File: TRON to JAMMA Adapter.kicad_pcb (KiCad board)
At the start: 2 copper layers, 111 x 98.7 mm, 58 parts, among them P1 1K, P2 10K, P3 1K, U1 74LS86, U2A 74LS191, U2B 74LS191, U3 NE555, U4 LM386, U5 NE555

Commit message: move connectors up, rework vias a bit, update text
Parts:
- moved MCRJ2 3.80 mm to (153.8, 66.6)
- moved MCRJ3 3.80 mm to (168.8, 66.6)
- moved MCRJ4A 3.80 mm to (98.0, 66.6)
- moved MCRJ4B 3.80 mm to (118.2, 66.6)
- moved MCRJ5 3.80 mm to (138.6, 66.6)
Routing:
- net 1P_U: track 30.5 -> 24.9 mm
- net VOL_GND: track 33.0 -> 38.3 mm
- net 1P_B1: track 30.2 -> 25.4 mm
- net 2P_START: track 49.6 -> 45.4 mm
- net 1P_D: track 32.0 -> 28.1 mm
- net E3: track 32.3 -> 36.1 mm
- net VOL_IN: track 30.6 -> 34.4 mm
- net VIDEO_RED: track 19.9 -> 16.1 mm
- net VOL_OUT: track 27.6 -> 31.4 mm
- net VIDEO_VSYNC: track 76.5 -> 80.3 mm
- net VIDEO_G: track 20.0 -> 16.2 mm
- net E4: track 32.7 -> 36.5 mm
- net E2: track 31.3 -> 35.1 mm
- net AUDIO_R: track 41.6 -> 45.4 mm
- net E1: track 30.7 -> 34.5 mm
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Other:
- board text added: "Bally/Midway MCR II JAMMA Interface for TRON^{TM}, Discs of TRON^{TM}, Rev. 1"
- board text added: "COIN 1"
- board text added: "COIN 2"
- board text removed: "Bally/Midway MCR JAMMA Interface, Rev. 1 for TRON^{TM}, Discs of TRON^{TM}"
- board text removed: "C1"
- board text removed: "C2"

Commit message: slightly widen
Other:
- board size 111 x 98.7 mm -> 111.6 x 98.7 mm
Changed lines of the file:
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@@
 	(gr_poly
 		(pts
-			(xy 173.5 56.550005) (xy 176 56.550005) (xy 176 45.05) (xy 200.500004 45.05) (xy 200.500004 68.050005)
-			(xy 200.5 68.050005) (xy 200.5 109.050005) (xy 200.5 143.75) (xy 89.5 143.75) (xy 89.5 109.050005)
-			(xy 89.499997 109.050005) (xy 89.499997 68.050005) (xy 89.499997 45.05) (xy 173.5 45.05)
+			(xy 173.5 56.550005) (xy 176 56.550005) (xy 176 45.05) (xy 200.700004 45.05) (xy 200.7 143.75) (xy 89.1 143.75)
+			(xy 89.099997 45.05) (xy 173.5 45.05)
 		)
 		(stroke

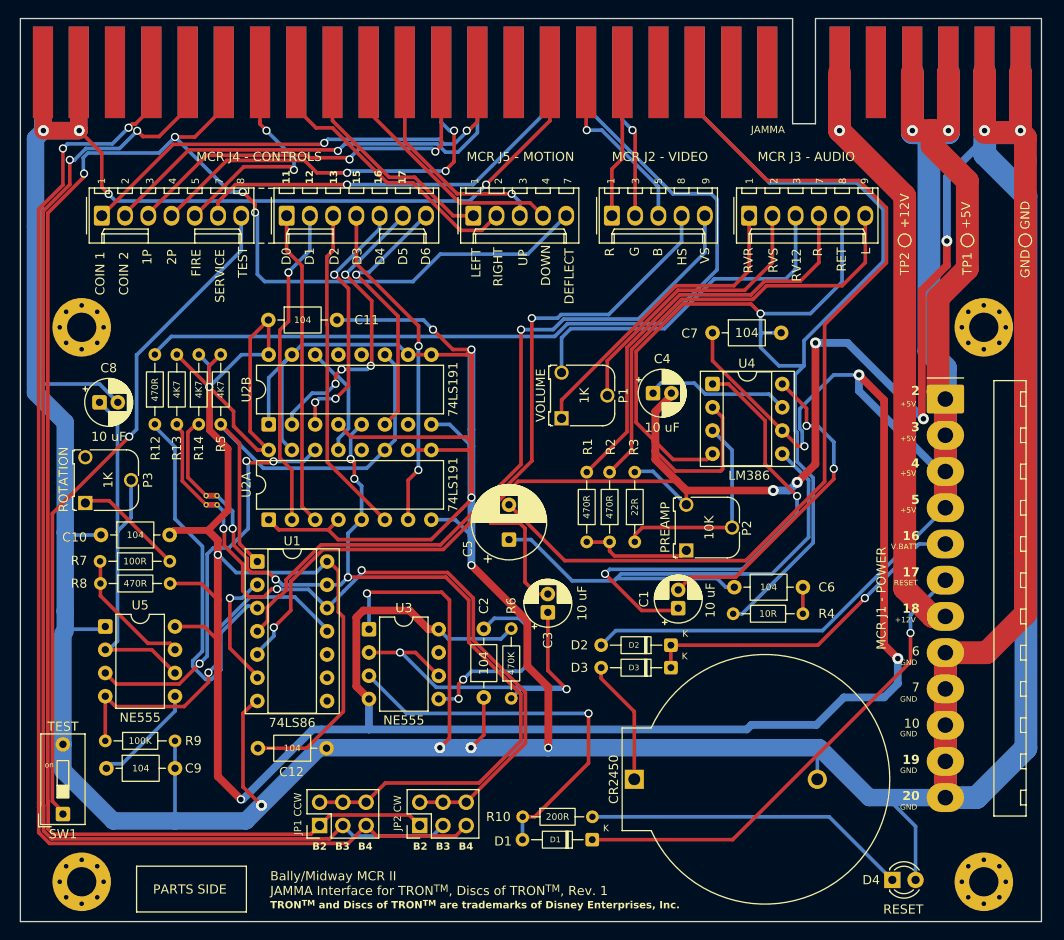
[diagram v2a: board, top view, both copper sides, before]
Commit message: slightly widen boards
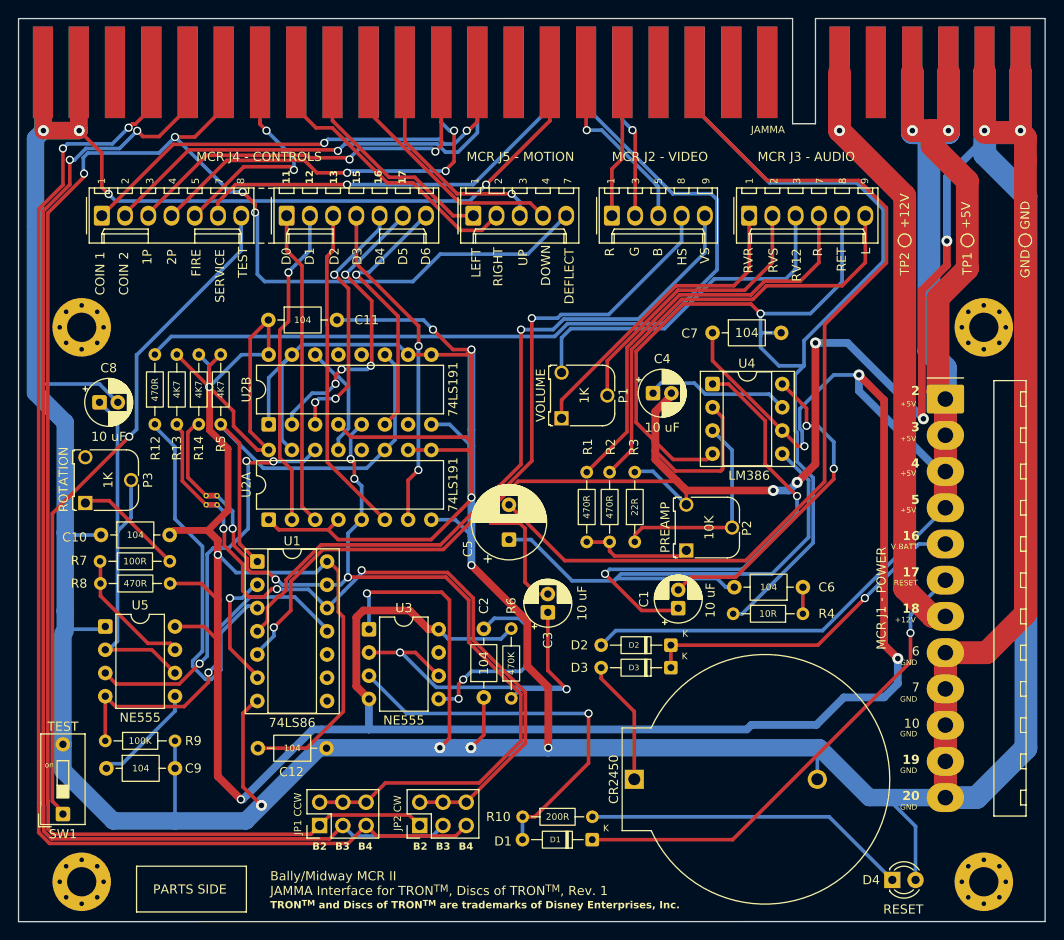
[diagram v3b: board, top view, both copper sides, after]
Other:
- board size 111.6 x 98.7 mm -> 112.2 x 98.7 mm
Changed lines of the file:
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@@
 	(gr_poly
 		(pts
-			(xy 173.5 56.550005) (xy 176 56.550005) (xy 176 45.05) (xy 200.700004 45.05) (xy 200.7 143.75) (xy 89.1 143.75)
-			(xy 89.099997 45.05) (xy 173.5 45.05)
+			(xy 173.5 56.550005) (xy 176 56.550005) (xy 176 45.05) (xy 201.100004 45.05) (xy 201.1 143.75) (xy 88.897213 143.757185)
+			(xy 88.89721 45.057185) (xy 173.5 45.05)
 		)
 		(stroke

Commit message: chamma compat, add b5/b6 and pins for level up/dn on dot
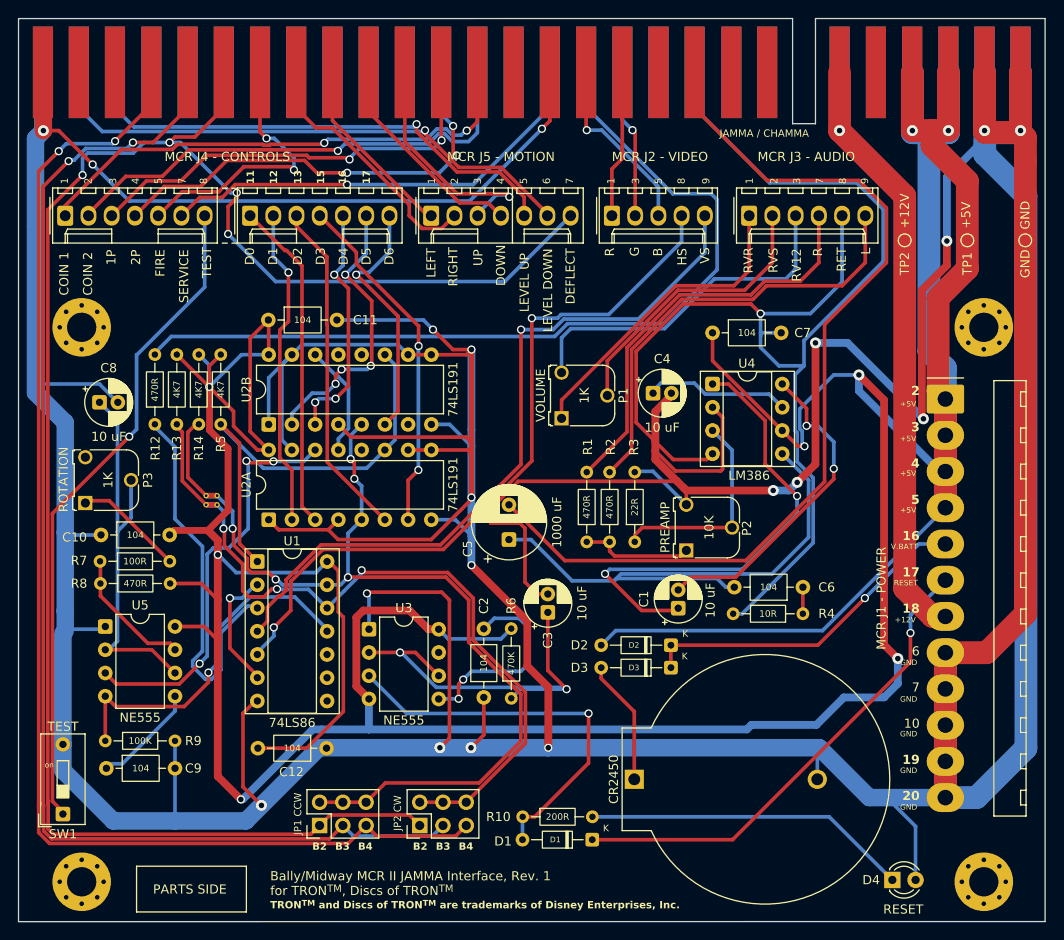
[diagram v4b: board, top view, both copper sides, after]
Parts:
- JAMMA / CHAMMA: renamed from JAMMA
- MCRJ5: value Molex_KK-254_AE-6410-05A_1x05_P2.54mm_Vertical -> Molex_KK-254_AE-6410-07A_1x07_P2.54mm_Vertical; footprint Connector_Molex:Molex_KK-254_AE-6410-05A_1x05_P2.54mm_Vertical -> Connector_Molex:Molex_KK-254_AE-6410-07A_1x07_P2.54mm_Vertical
- moved MCRJ5 4.60 mm to (134.0, 66.6)
- moved MCRJ4A 4.00 mm to (94.0, 66.6)
- moved MCRJ4B 4.00 mm to (114.2, 66.6)
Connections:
- JAMMA / CHAMMA pad 27: GND -> (no net)
- JAMMA / CHAMMA pad d: (no net) -> 1P_B5
- JAMMA / CHAMMA pad e: GND -> 1P_B6
- MCRJ5 pad 5: 1P_B2 -> 1P_B5
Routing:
- net 1P_B6: track 0.00 -> 60.4 mm, vias 0 -> 1
- net 1P_B5: track 0.00 -> 55.4 mm, vias 0 -> 1
- net GND: track 1050.7 -> 1031.6 mm, vias 21 -> 20
- net COIN_1: track 51.3 -> 56.0 mm
- net 1P_D: track 28.1 -> 23.5 mm
- net 1P_L: track 25.0 -> 20.4 mm
- net 1P_B1: track 25.4 -> 29.9 mm
- net 1P_R: track 34.1 -> 30.0 mm
- net COIN_2: track 49.8 -> 53.8 mm
- net 2P_START: track 45.4 -> 49.0 mm
- net 1P_START: track 44.1 -> 47.4 mm
- net SERVICE_SW: track 45.9 -> 49.0 mm
- net E1: track 34.5 -> 36.3 mm
- net 1P_U: track 24.9 -> 26.7 mm
- net E7: track 29.2 -> 27.5 mm
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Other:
- board text added: "Bally/Midway MCR II JAMMA Interface, Rev. 1 for TRON^{TM}, Discs of TRON^{TM}"
- board text added: "LEVEL DOWN"
- board text added: "LEVEL UP"
- board text removed: "Bally/Midway MCR II JAMMA Interface for TRON^{TM}, Discs of TRON^{TM}, Rev. 1"

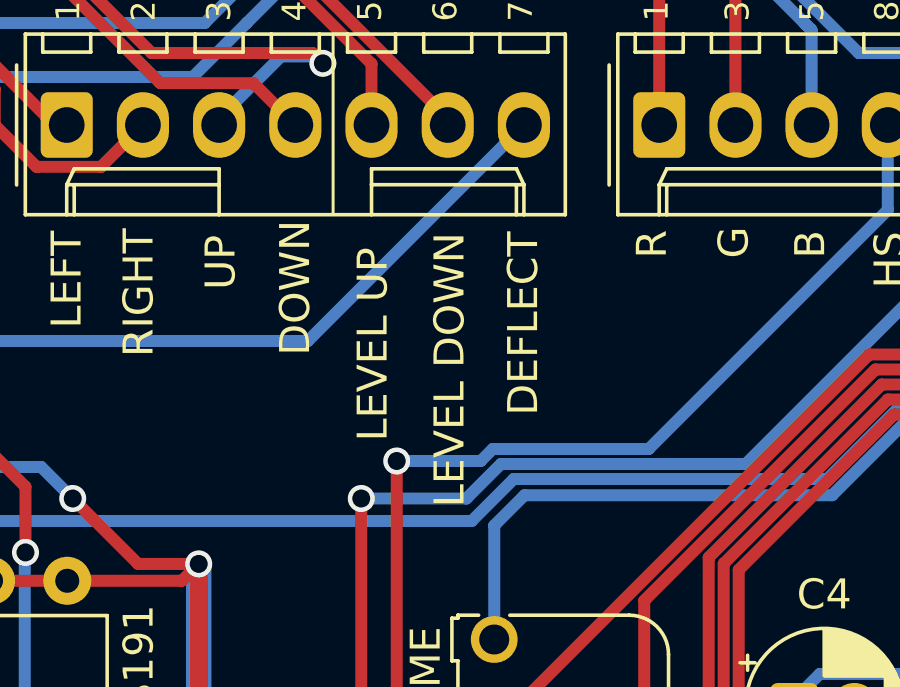
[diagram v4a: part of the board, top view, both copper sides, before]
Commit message: silkscreen tweaks
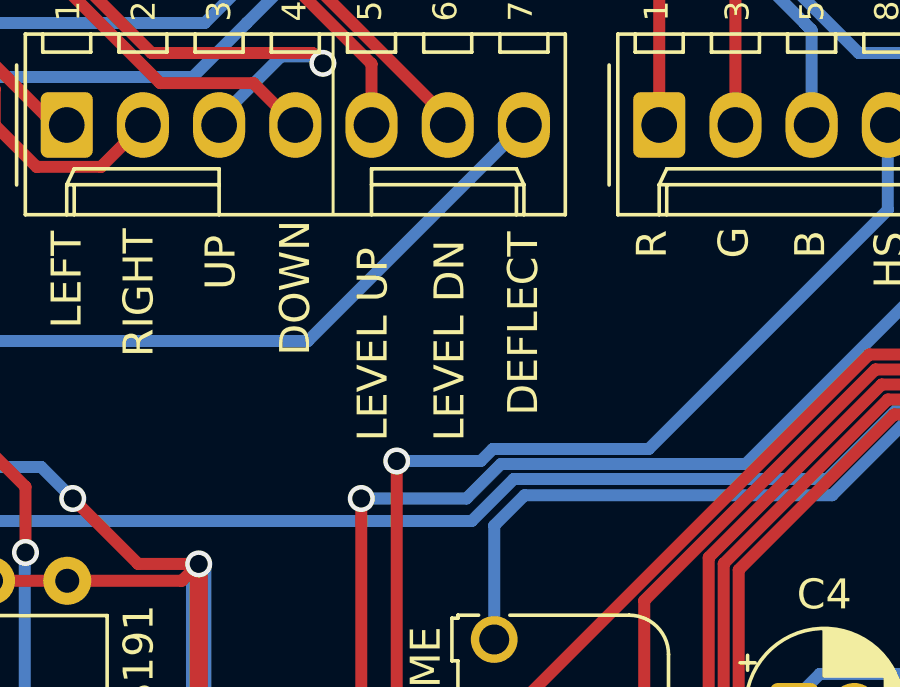
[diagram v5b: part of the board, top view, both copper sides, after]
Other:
- board text added: "LEVEL DN"
- board text removed: "LEVEL DOWN"
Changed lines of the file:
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@@
 		)
 	)
-	(gr_text "LEVEL DOWN"
-		(at 147.345904 79.333334 90)
+	(gr_text "LEVEL DN"
+		(at 147.345904 77.142858 90)
 		(layer "F.SilkS")
 		(effects

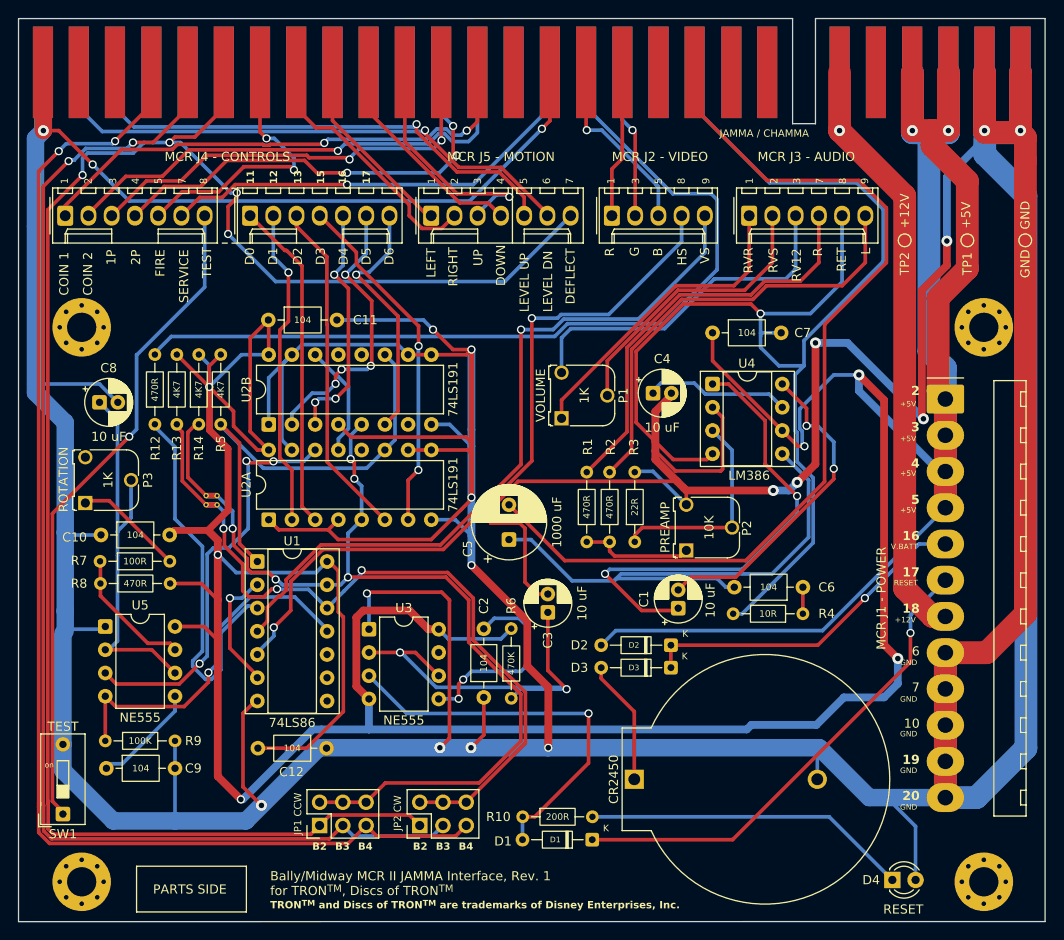
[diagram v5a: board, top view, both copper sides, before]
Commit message: remove D6/E7
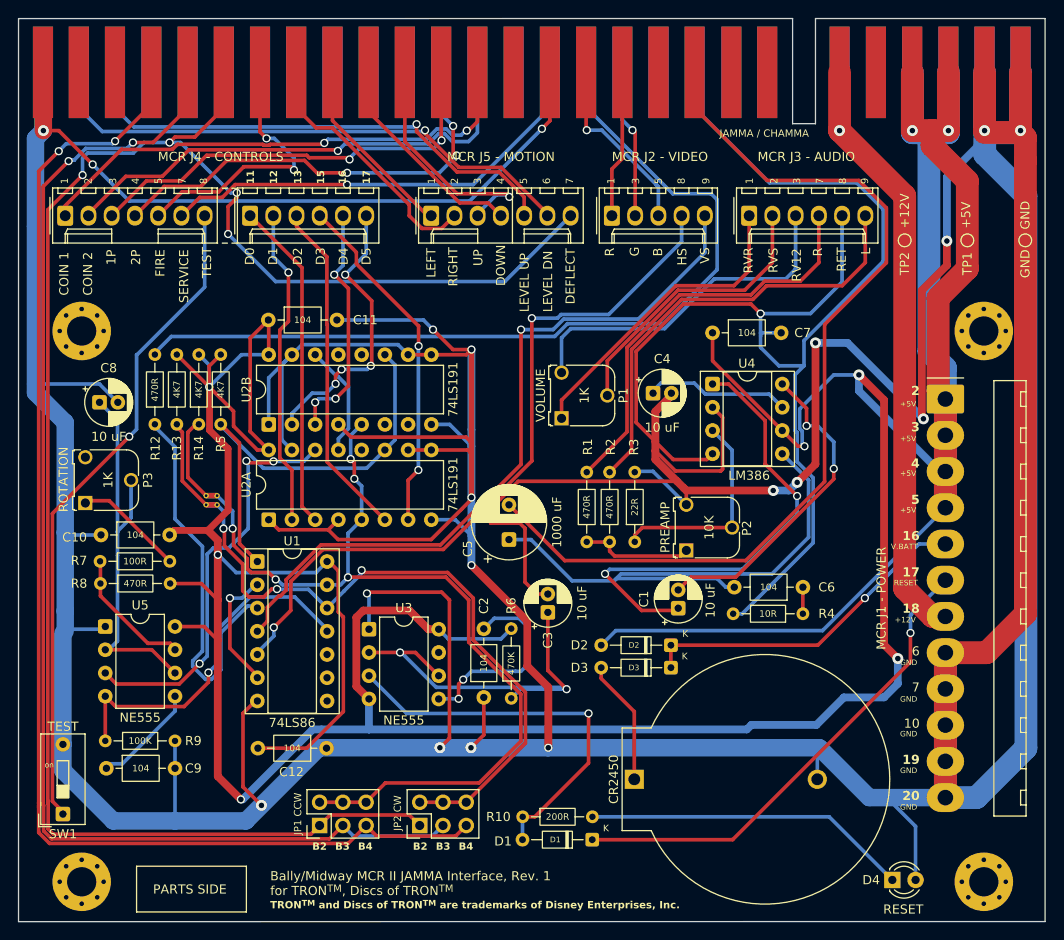
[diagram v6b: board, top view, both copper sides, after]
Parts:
- MCRJ4B: value Molex_KK-254_AE-6410-07A_1x07_P2.54mm_Vertical -> Molex_KK-254_AE-6410-06A_1x06_P2.54mm_Vertical; footprint Connector_Molex:Molex_KK-254_AE-6410-07A_1x07_P2.54mm_Vertical -> Connector_Molex:Molex_KK-254_AE-6410-06A_1x06_P2.54mm_Vertical
- moved PMH1 0.40 mm to (194.4, 79.2)
- moved PMH4 0.40 mm to (95.8, 79.2)
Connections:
- U2B pad 6: E7 -> (no net)
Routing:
- net E7: track 27.5 -> 0.00 mm, vias 1 -> 0
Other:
- board text removed: "D6"

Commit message: minor silkscreen tweaks, new snapshots
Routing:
- net VIDEO_VSYNC: track 80.3 -> 81.0 mm
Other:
- board text added: "DOT"
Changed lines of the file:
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@@
 	)
 	(gr_line
+		(start 145 78.8)
+		(end 143.4 78.8)
+		(stroke
+			(width 0.076)
+			(type default)
+		)
+		(layer "F.SilkS")
+	)
+	(gr_line
 		(start 112.82 69.6)
 		(end 110.62 69.6)
@@
 	)
 	(gr_line
+		(start 143.4 78.8)
+		(end 143.4 78.098063)
+		(stroke
+			(width 0.076)
+			(type default)
+		)
+		(layer "F.SilkS")
+	)
+	(gr_line
 		(start 142.878735 63.576849)
 		(end 142.878735 69.576849)
@@
 		(layer "F.SilkS")
 	)
+	(gr_line
+		(start 150 78.8)
+		(end 148.4 78.8)
+		(stroke
+			(width 0.076)
+			(type default)
+		)
+		(layer "F.SilkS")
+	)
+	(gr_line
+		(start 150 78.8)
+		(end 150 78.098063)
+		(stroke
+			(width 0.076)
+			(type default)
+		)
+		(layer "F.SilkS")
+	)
 	(gr_poly
 		(pts
@@
 		)
 	)
+	(gr_text "DOT"
+		(at 145.581535 78.964521 0)
+		(layer "F.SilkS")
+		(effects
+			(font
+				(size 0.76 0.76)
+				(thickness 0.114)
+			)
+			(justify left bottom)
+		)
+	)
 	(gr_text "HS"
 		(at 162.014673 72.047619 90)
@@
 	)
 	(segment
-		(start 118.15 106.385843)
-		(end 121.956843 102.579)
+		(start 135.021 102.579)
+		(end 142.6 95)
 		(width 0.4)
 		(layer "F.Cu")
@@
 	)
 	(segment
-		(start 117.52698 108.155749)
-		(end 118.15 107.532729)
+		(start 142.6 95)
+		(end 142.6 78.8)
 		(width 0.4)
 		(layer "F.Cu")
@@
 	)
 	(segment
-		(start 117.351358 108.155749)
-		(end 117.52698 108.155749)
+		(start 115 112.02)
+		(end 118.15 108.87)
 		(width 0.4)
 		(layer "F.Cu")
@@
 	)
 	(segment
-		(start 118.15 107.532729)
+		(start 118.15 108.87)
 		(end 118.15 106.385843)
 		(width 0.4)
@@
 	)
 	(segment
-		(start 116.101 110.919)
-		(end 116.101 109.406107)
-		(width 0.4)
-		(layer "F.Cu")
-		(net 22)
-	)
-	(segment
-		(start 116.101 109.406107)
-		(end 117.351358 108.155749)
-		(width 0.4)
-		(layer "F.Cu")
-		(net 22)
-	)
-	(segment
-		(start 143.818376 93.781624)
-		(end 143.818376 79.05)
+		(start 118.15 106.385843)
+		(end 121.956843 102.579)
 		(width 0.4)
 		(layer "F.Cu")
@@
 		(net 22)
 	)
-	(segment
-		(start 115 112.02)
-		(end 116.101 110.919)
-		(width 0.4)
-		(layer "F.Cu")
-		(net 22)
-	)
-	(segment
-		(start 135.021 102.579)
-		(end 143.818376 93.781624)
-		(width 0.4)
-		(layer "F.Cu")
-		(net 22)
-	)
 	(via
-		(at 143.818376 79.05)
+		(at 142.6 78.8)
 		(size 0.9)
 		(drill 0.6)
@@
 	)
 	(segment
-		(start 163.91 70.625)
-		(end 156.635 77.9)
+		(start 148.475104 77.9)
+		(end 147.575104 78.8)
 		(width 0.4)
 		(layer "B.Cu")
@@
 	)
 	(segment
-		(start 147.325104 79.05)
-		(end 143.818376 79.05)
+		(start 156.635 77.9)
+		(end 148.475104 77.9)
 		(width 0.4)
 		(layer "B.Cu")
@@
 	)
 	(segment
-		(start 148.475104 77.9)
-		(end 147.325104 79.05)
+		(start 163.91 70.625)
+		(end 156.635 77.9)
 		(width 0.4)
 		(layer "B.Cu")
@@
 	)
 	(segment
-		(start 156.635 77.9)
-		(end 148.475104 77.9)
+		(start 147.575104 78.8)
+		(end 142.6 78.8)
 		(width 0.4)
 		(layer "B.Cu")

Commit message: miscellaneous alignment tweaks
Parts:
- moved MCRJ4B 0.13 mm to (114.3, 66.6)
